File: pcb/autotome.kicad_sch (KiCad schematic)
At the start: 150 parts, among them J1 Conn_01x01_Pin, J10 Conn_01x01_Pin, J11 Conn_01x01_Pin, J12 Conn_01x01_Pin, J13 Conn_01x01_Pin, J14 Conn_01x01_Pin, J15 Conn_01x01_Pin, J16 Conn_01x01_Pin, J17 Conn_01x01_Pin, J18 Conn_01x01_Pin, J19 Conn_01x01_Pin, J2 Conn_01x01_Pin, J20 Conn_01x01_Pin, J21 Conn_01x01_Pin, J22 Conn_01x01_Pin, J23 Conn_01x01_Pin, J24 Conn_01x01_Pin, J25 Conn_01x01_Pin, J26 Conn_01x01_Pin, J27 Conn_01x01_Pin, J28 Conn_01x01_Pin, J3 Conn_01x01_Pin, J4 Conn_01x01_Pin, J5 Conn_01x01_Pin, J6 Conn_01x01_Pin, J7 Conn_01x01_Pin, J8 Conn_01x01_Pin, J9 Conn_01x01_Pin, SW1 SW_PUSH, SW10 SW_PUSH, SW11 SW_PUSH, SW12 SW_PUSH, SW13 SW_PUSH, SW14 SW_PUSH, SW15 SW_PUSH, SW16 SW_PUSH, SW17 SW_PUSH, SW18 SW_PUSH, SW19 SW_PUSH, SW2 SW_PUSH, SW20 SW_PUSH, SW21 SW_PUSH, SW22 SW_PUSH, SW23 SW_PUSH, SW24 SW_PUSH, SW25 SW_PUSH, SW26 SW_PUSH, SW27 SW_PUSH, SW28 SW_PUSH, SW29 SW_PUSH, SW3 SW_PUSH, SW30 SW_PUSH, SW31 SW_PUSH, SW32 SW_PUSH, SW33 SW_PUSH, SW34 SW_PUSH, SW35 SW_PUSH, SW36 SW_PUSH, SW37 SW_PUSH, SW38 SW_PUSH, SW39 SW_PUSH, SW4 SW_PUSH, SW40 SW_PUSH, SW41 SW_PUSH, SW42 SW_PUSH, SW43 SW_PUSH, SW44 SW_PUSH, SW45 SW_PUSH, SW46 SW_PUSH, SW47 SW_PUSH, SW48 SW_PUSH, SW49 SW_PUSH, SW5 SW_PUSH, SW50 SW_PUSH, SW51 SW_PUSH, SW52 SW_PUSH, SW53 SW_PUSH, SW54 SW_PUSH, SW55 SW_PUSH, SW56 SW_PUSH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

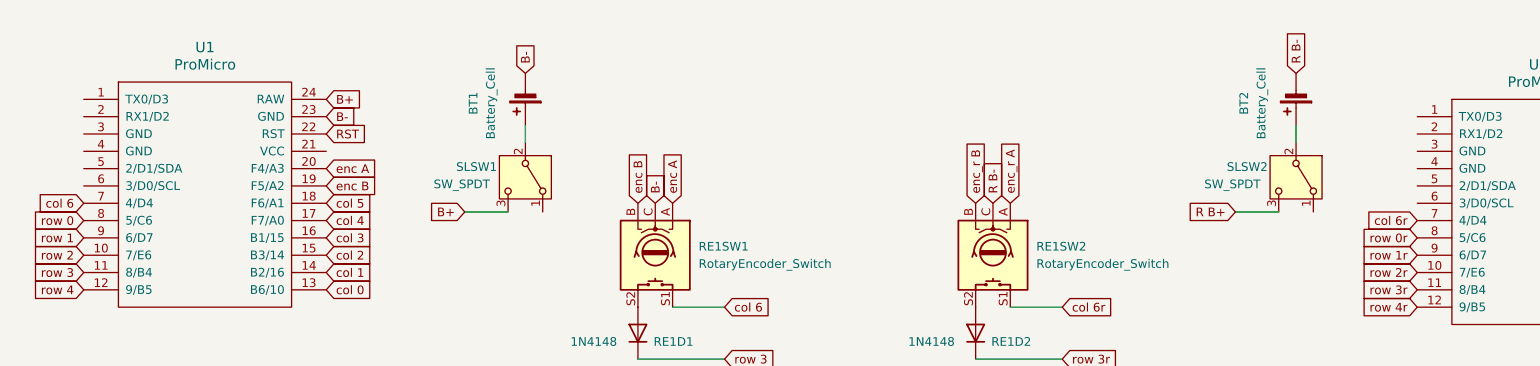
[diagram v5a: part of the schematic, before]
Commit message: add b- to all GNDs in controller
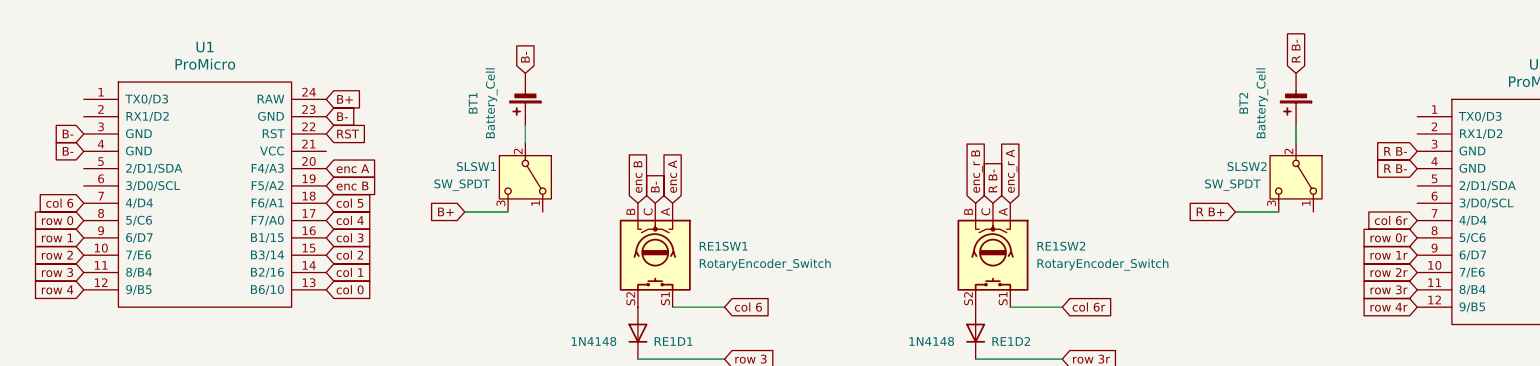
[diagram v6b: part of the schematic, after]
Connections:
- net B-: now also U1.3 (GND), U1.4 (GND)
- net R B-: now also U2.3 (GND), U2.4 (GND)
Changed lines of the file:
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@@
+		)
+	)
+	(global_label "R B-"
+		(shape input)
+		(at 227.33 41.91 180)
+		(fields_autoplaced yes)
+		(effects
+			(font
+				(size 1.27 1.27)
+			)
+			(justify right)
+		)
+		(property "Intersheetrefs" "${INTERSHEET_REFS}"
+			(at 219.2648 41.91 0)
+			(hide yes)
+			(show_name no)
+			(do_not_autoplace no)
+			(effects
+				(font
+					(size 1.27 1.27)
+				)
+				(justify right)
+			)
 		)
 	)
@@
 		)
 	)
+	(global_label "R B-"
+		(shape input)
+		(at 227.33 44.45 180)
+		(fields_autoplaced yes)
+		(effects
+			(font
+				(size 1.27 1.27)
+			)
+			(justify right)
+		)
+		(property "Intersheetrefs" "${INTERSHEET_REFS}"
+			(at 219.2648 44.45 0)
+			(hide yes)
+			(show_name no)
+			(do_not_autoplace no)
+			(effects
+				(font
+					(size 1.27 1.27)
+				)
+				(justify right)
+			)
+		)
+	)
 	(global_label "enc_r B"
 		(shape input)
@@
 		)
 	)
+	(global_label "B-"
+		(shape input)
+		(at 31.75 39.37 180)
+		(fields_autoplaced yes)
+		(effects
+			(font
+				(size 1.27 1.27)
+			)
+			(justify right)
+		)
+		(property "Intersheetrefs" "${INTERSHEET_REFS}"
+			(at 25.9224 39.37 0)
+			(hide yes)
+			(show_name no)
+			(do_not_autoplace no)
+			(effects
+				(font
+					(size 1.27 1.27)
+				)
+				(justify right)
+			)
+		)
+	)
 	(global_label "row 4"
 		(shape input)
@@
 			)
 		)
+	)
+	(global_label "B-"
+		(shape input)
+		(at 31.75 41.91 180)
+		(fields_autoplaced yes)
+		(effects
+			(font
+				(size 1.27 1.27)
+			)
+			(justify right)
+		)
+		(property "Intersheetrefs" "${INTERSHEET_REFS}"
+			(at 25.9224 41.91 0)
+			(hide yes)
+			(show_name no)
+			(do_not_autoplace no)
+			(effects
+				(font
+					(size 1.27 1.27)
+				)
+				(justify right)
+			)
+		)

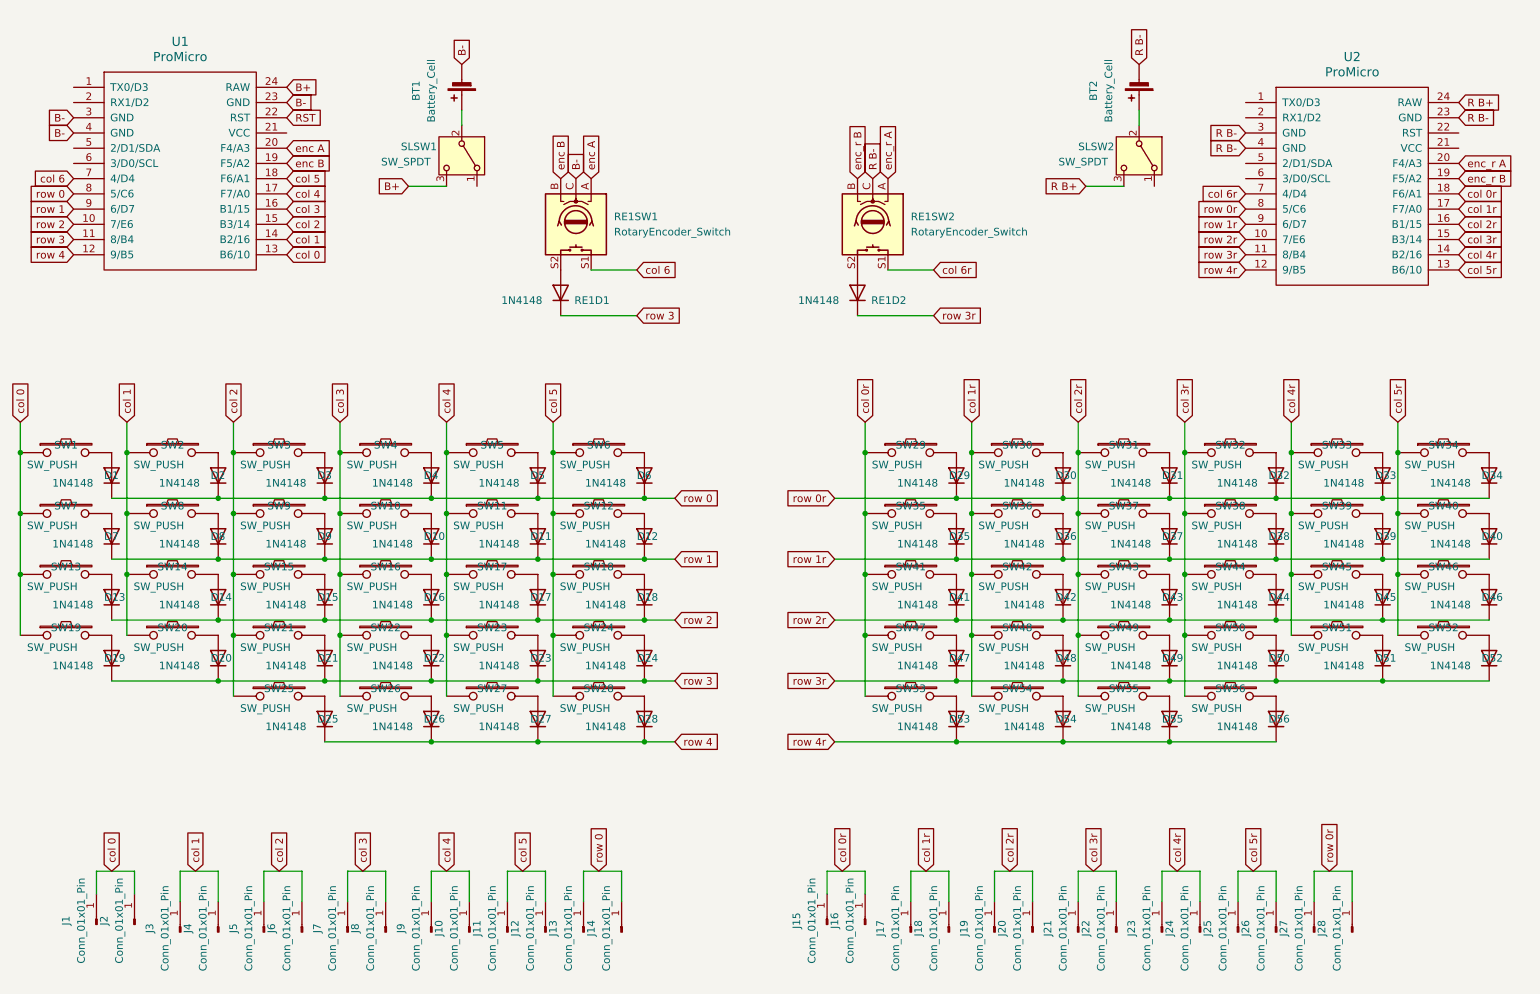
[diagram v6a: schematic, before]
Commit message: remove reconnection pads, only keep row1 pads
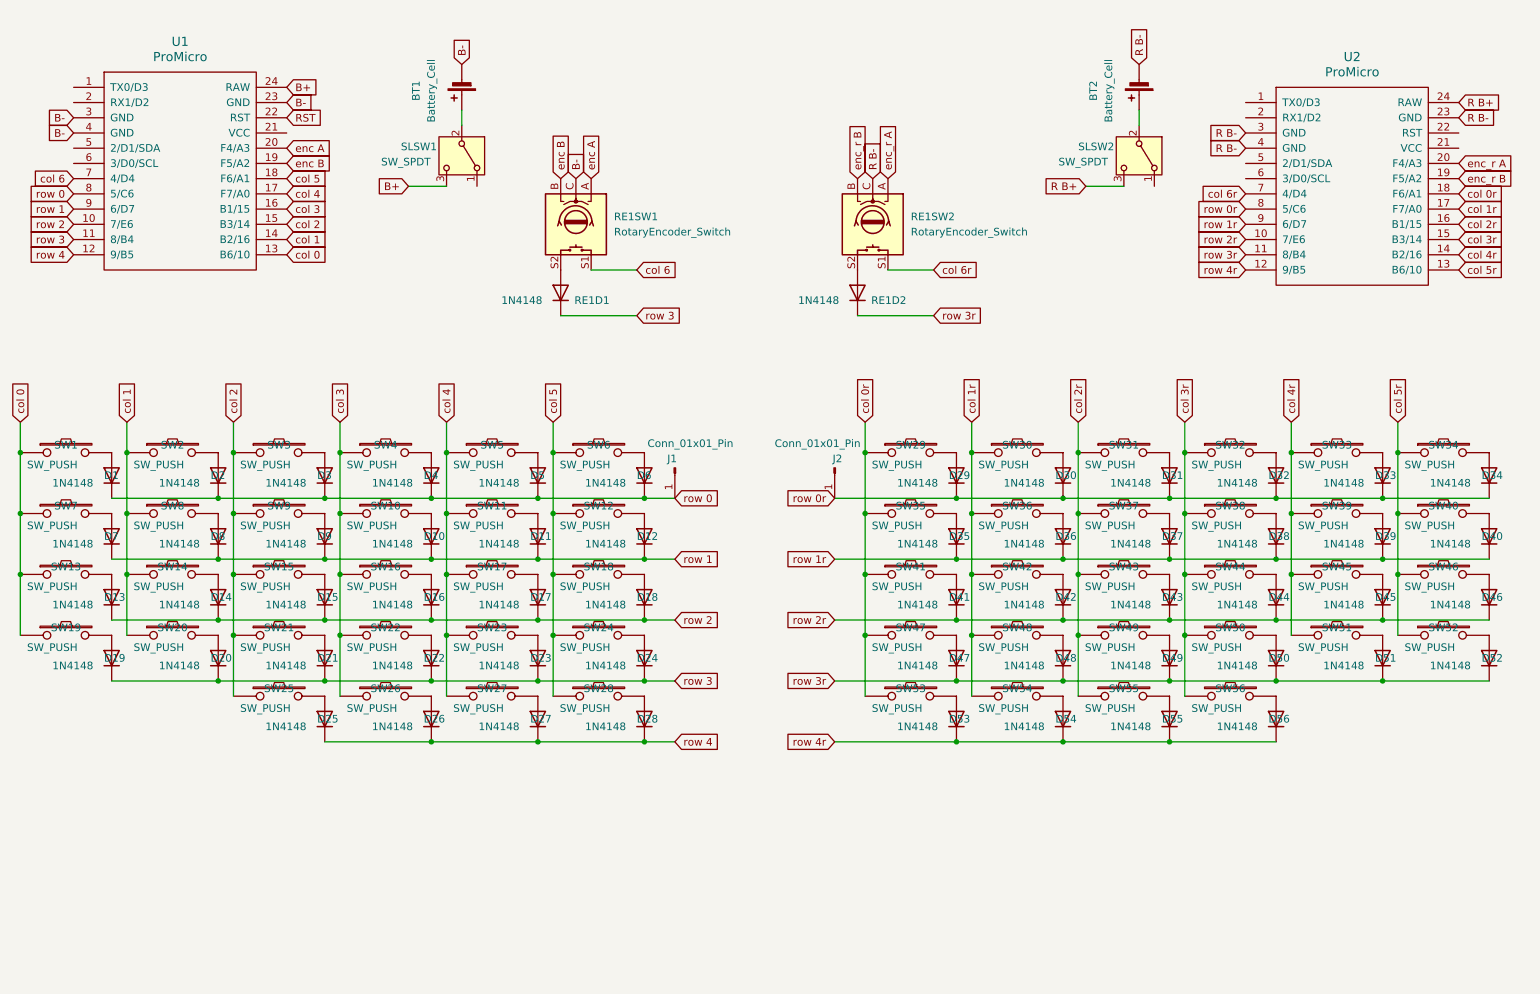
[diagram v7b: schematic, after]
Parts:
- removed J1, J10, J11, J12, J13, J15, J16, J17, J18, J19, J2, J20, J21, J22, J23, J24, J25, J26, J27, J3, J4, J5, J6, J7, J8, J9: Conn_01x01_Pin, TestPoint:TestPoint_THTPad_1.0x1.0mm_Drill0.5mm, symbol Connector:Conn_01x01_Pin
- renumbered J14 to J1, J28 to J2
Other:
- moved on the sheet: J1, J2
